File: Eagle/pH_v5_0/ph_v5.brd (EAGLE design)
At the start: 100 x 84.6 mm, 101 parts, among them CON1 JACK_DC_BARREL, IC1 MCP1703DB, J1 RJ12RIGHTANGLE-I2C, J2 RJ12RIGHTANGLE-I2C, Q1 BSP75, Q2 BSP75, Q3 BSP75, Q4 BSP75, U1 HX711, U100 RN2483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

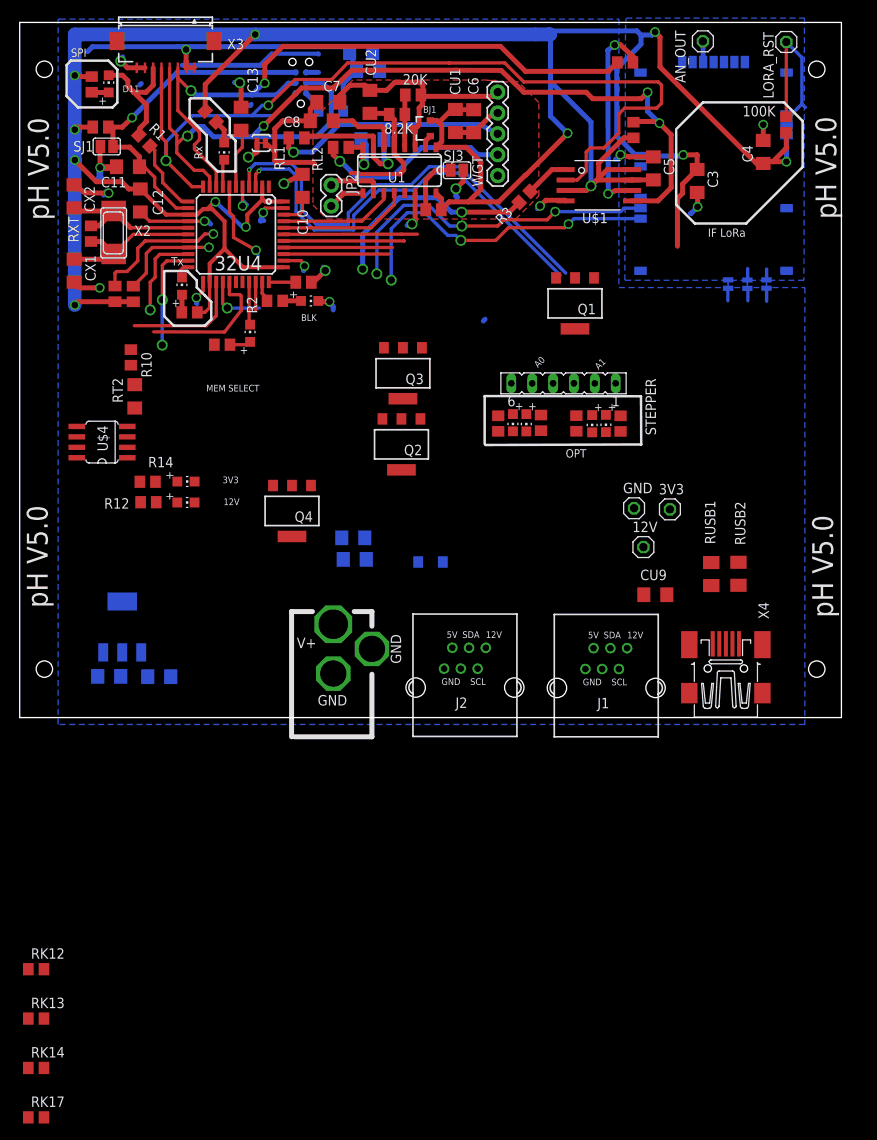
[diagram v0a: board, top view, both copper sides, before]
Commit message: started design of the phv5.0 board, conductommetry is still missing, stepper to be rerouted to use one single port would be better !
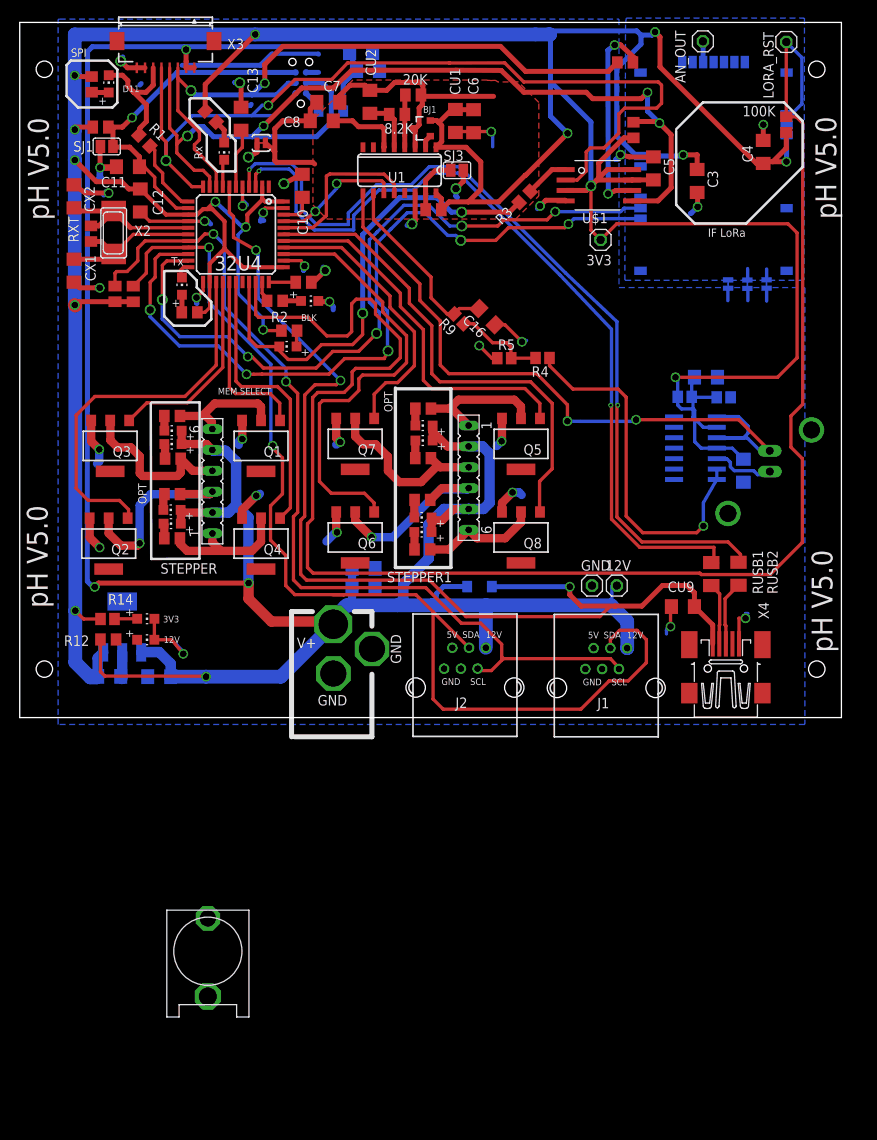
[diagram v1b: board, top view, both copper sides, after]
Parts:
- removed C9: 100nF, rcl:C1206
- removed JP2: (no value), SparkFun-Connectors:1X02
- removed R10: 1K, rcl:R0805
- removed RL1, RL2: 100, resistor:M0805
- removed RT2: 4.7k, resistor:R1206
- removed U$4: DS18B20, lpatiny:SO8
- removed WGT: (no value), SparkFun-Connectors:1X05
- added C14, C15: 100n, rcl:C1206
- added C16: 22uF, rcl:C1206
- added IC2: TL084D, linear:SO14
- added LDM5, LDM6, LDM7, LDM8: RED, adafruit:CHIP-LED0805
- added Q5, Q6, Q7, Q8: BSP75, infineon:PG-SOT-223
- added R4, R5, R9: 2.2k, resistor:R0805
- added R6, R8: 100k, resistor:R0805
- added STEPPER1: (no value), con-lsta:FE06
- added U$2: BNC-VERTICAL, phMeter:BNC-VERTICAL
- added U$3: VERTICAL-JACK, phMeter:VERTICAL-JACK
- moved RK14 83.6 mm to (44.0, 23.6), turned to 180 degrees
- moved RK17 83.6 mm to (44.0, 17.6), turned to 180 degrees
- moved RK12 82.9 mm to (44.1, 34.7), turned to 180 degrees
- moved RK13 82.9 mm to (44.1, 28.7), turned to 180 degrees
- moved RK8 56.3 mm to (13.5, 18.9), turned to 180 degrees
- moved LDM4 54.2 mm to (13.6, 20.7), turned to 90 degrees
- moved LDM3 52.2 mm to (13.5, 22.4), turned to 90 degrees
- moved RK9 49.9 mm to (13.6, 24.3), turned to 180 degrees
- moved RK10 45.0 mm to (13.6, 28.6), turned to 180 degrees
- moved STEPPER 44.4 mm to (18.4, 25.9), turned to 90 degrees
- moved LDM2 43.1 mm to (13.6, 30.4), turned to 90 degrees
- moved Q1 42.0 mm to (24.4, 30.2)
- moved LDM1 41.4 mm to (13.7, 32.0), turned to 90 degrees
- moved RK11 39.7 mm to (13.6, 33.8), turned to 180 degrees
- moved Q2 37.6 mm to (5.82, 18.3)
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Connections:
- removed net 5: J1.+5V, J2.+5V
- removed net N$20: C9.2, RL1.1, U1.7
- removed net N$43: C9.1, RL2.1, U1.8
- new net N$11: LDM6.C, RK13.2
- new net N$12: LDM7.C, RK14.2
- new net N$13: LDM8.C, RK17.2
- new net N$17: R4.2, R5.2, R9.1
- new net N$2: Q5.2, RK12.1, STEPPER1.1
- new net N$21: IC2.5, U$2.S
- new net N$27: C15.2, IC2.2, R6.1, R8.2
- new net N$28: IC2.6, IC2.7, R4.1
- new net N$4: Q7.2, RK13.1, STEPPER1.3
- new net N$6: Q6.2, RK14.1, STEPPER1.4
- new net N$8: Q8.2, RK17.1, STEPPER1.6
- net +12V: now also LDM5.A, LDM6.A, LDM7.A, LDM8.A, STEPPER1.2, STEPPER1.5
- net 3.3V: now also C14.1, IC2.4, R6.2; no longer RT2.1, U$4.3
- net A+: now also U1.8; no longer RL2.2, WGT.2
- net A-: now also U1.7; no longer RL1.2, WGT.3
- net A0: now also Q6.1; no longer Q2.1, RK13.2
- net A1: now also Q7.1; no longer Q4.1, RK17.2
- net A2: now also Q5.1; no longer Q3.1, RK14.2
- net A3: now also Q8.1; no longer Q1.1, RK12.2
- net A6: now also Q2.1
- net B+: now also C16.2, R9.2; no longer JP2.1
- net B-: now also IC2.1, IC2.3, U$2.G; no longer JP2.2
- net D12*: now also Q3.1
- net D6*: now also Q1.1; no longer R10.1
- net D8*: now also Q4.1
- net GND: now also C14.2, C15.1, C16.1, IC2.11, Q5.3, Q6.3, Q7.3, Q8.3, R5.1, R8.1; no longer RK12.1, RK13.1, RK14.1, RK17.1, U$4.5, WGT.1, WGT.4
- net N$5: no longer WGT.5
- net N$9: now also LDM5.C, RK12.2; no longer R10.2, RT2.2, U$4.4
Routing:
- net +12V: track 44.0 -> 323.9 mm, vias 1 -> 4
- net D5*: track 23.8 -> 202.5 mm
- net 3.3V: track 351.4 -> 491.0 mm, vias 12 -> 15
- net VUSB: track 10.2 -> 132.4 mm, vias 1 -> 3
- net SDA: track 12.6 -> 134.2 mm, vias 1 -> 2
- net SCL: track 16.6 -> 112.1 mm, vias 1 -> 2
- net B-: track 4.50 -> 86.8 mm, vias 0 -> 2
- net GND: track 105.7 -> 167.8 mm, vias 18 -> 32
- net USB_P: track 55.6 -> 106.2 mm, vias 1 -> 2
- net USB_N: track 53.6 -> 101.9 mm, vias 1 -> 2
- net N$28: track 0.00 -> 44.3 mm, vias 0 -> 1
- net RX: track 50.7 -> 94.6 mm, vias 4 -> 5
- net A3: track 16.3 -> 59.6 mm
- net A0: track 12.8 -> 54.9 mm
- net TX: track 53.5 -> 88.9 mm
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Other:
- board text removed: "A0"
- board text removed: "A1"

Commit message: ph board v5, need to be checked, to provide pin mapping and gerbers
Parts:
- removed RK15: 10k, rcl:R0805
- removed SJ5: (no value), SparkFun-Passives:PAD-JUMPER-2-NC_BY_TRACE_YES_SILK
- removed TXLD: RED, adafruit:CHIP-LED0805
- added B1: MB1S, rectifier:SOIC-4
- added C17, C18, C19, C20, C24, C9: 100nF, SparkysWidgets:1206
- added C21, C22, C23: 1uF, SparkysWidgets:1206
- added D3, D5: 4148, SparkysWidgets:SOD123
- added IC3: TL084D, linear:SO14
- added IC5: TPS60400DBV, SparkysWidgets:SOT23-DBV
- added R10: 22K, SparkysWidgets:0805
- added R11, R13, R15, R16, R17, R18, R20, R21, R22, R23, R24: 1K, SparkysWidgets:0805
- added R19: 1k, resistor:R0805
- added R7: 10K, SparkysWidgets:0805
- added TP5: OSCVout, SW_Passives:PAD.03X.03
- added U$5: BNC-VERTICAL, phMeter:BNC-VERTICAL
- moved U$3 85.4 mm to (87.3, 15.7)
- moved 3V3 26.2 mm to (57.9, 80.2)
- moved SJ6 18.0 mm to (68.3, 53.7), turned to 180 degrees
- moved SJ4 16.5 mm to (68.2, 56.0), turned to 180 degrees
- moved IC2 9.72 mm to (70.3, 23.1)
- moved C14 9.03 mm to (76.4, 21.1)
- moved C15 8.70 mm to (81.3, 30.3)
- moved R8 8.14 mm to (81.7, 28.0)
- moved R6 6.98 mm to (77.3, 29.3), turned to 90 degrees
- moved R4 5.04 mm to (53.6, 40.8)
- moved R5 4.71 mm to (49.3, 40.8)
- moved RUSB1 2.55 mm to (80.3, 12.3)
- moved RUSB2 2.55 mm to (83.6, 12.3)
- moved U$2 2.52 mm to (78.3, 32.5)
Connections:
- removed net A-: U1.7
- new net -3V3: C22.2, IC3.11, IC5.1
- new net N$20: C9.1, R13.1
- new net N$26: C19.1, IC3.1, R10.2, R13.2, R15.1
- new net N$29: IC3.5, R15.2, R16.1, TP5.P$1
- new net N$30: C17.2, C9.2, IC3.3, R11.2
- new net N$35: IC3.6, R18.1, U$5.S
- new net N$36: C24.1, IC3.7, R18.2
- new net N$40: C24.2, IC3.10, R20.2
- new net N$43: B1.~2, IC3.8
- new net N$44: C19.2, D3.C, D5.A
- new net N$45: C21.1, IC5.3
- new net N$46: C21.2, IC5.5
- new net N$47: B1.-, C18.1, R17.1, R23.1
- new net N$48: B1.~1, IC3.9, R21.1
- new net N$49: B1.+, C18.2, R17.2, R22.1
- new net N$50: IC3.12, R22.2
- new net N$51: IC3.13, R23.2, R24.2
- net 3.3V: now also C20.1, C23.1, IC3.4, IC5.2, U$3.P$1; no longer RK15.1
- net A+: now also IC3.14, R24.1
- net A4: now also R19.1, U$3.P$2; no longer U1.12
- net ANGND: no longer SJ5.2
- net D7*: now also U1.12
- net D8*: no longer Q4.1
- net GND: now also C17.1, C20.2, C22.1, C23.2, IC5.4, R11.1, R16.2, R19.2, R20.1, R21.2, R7.1, U$5.G; no longer SJ5.1
- net LGND: now also U1.7
- net N$18: now also D3.A, D5.C, IC3.2, R10.1, R7.2; no longer RK15.2, TXLD.A
- net TXLED: now also Q4.1; no longer TXLD.C
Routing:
- net A4: track 20.5 -> 115.0 mm, vias 0 -> 3
- net A+: track 0.00 -> 52.8 mm, vias 0 -> 3
- net GND: track 167.8 -> 206.8 mm, vias 32 -> 35
- net N$29: track 0.00 -> 38.4 mm
- net TXLED: track 2.01 -> 39.1 mm, vias 0 -> 2
- net 3.3V: track 491.0 -> 526.2 mm, vias 15 -> 17
- net D8*: track 34.6 -> 0.00 mm
- net N$48: track 0.00 -> 27.4 mm, vias 0 -> 1
- net N$43: track 0.00 -> 26.7 mm, vias 0 -> 1
- net N$35: track 0.00 -> 22.8 mm, vias 0 -> 1
- net ANGND: track 7.79 -> 28.4 mm
- net D7*: track 0.00 -> 19.9 mm
- net B-: track 86.8 -> 106.1 mm
- net N$51: track 0.00 -> 17.2 mm, vias 0 -> 1
- net N$18: track 2.17 -> 18.7 mm
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
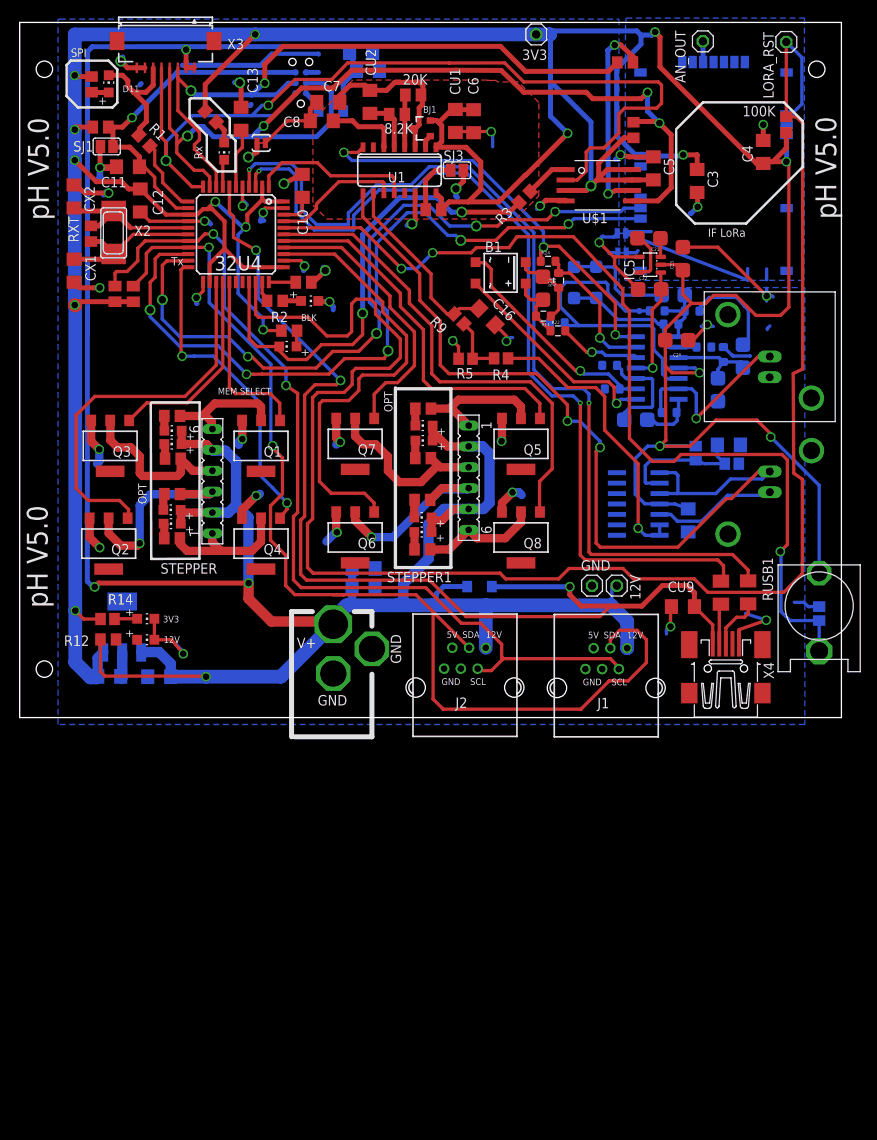
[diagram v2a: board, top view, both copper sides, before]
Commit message: finished phv5.0 board, need to dimension correctly the pH resistors and conductometry resistors and capa (not dimensionned yet !! careful not to solder anything)
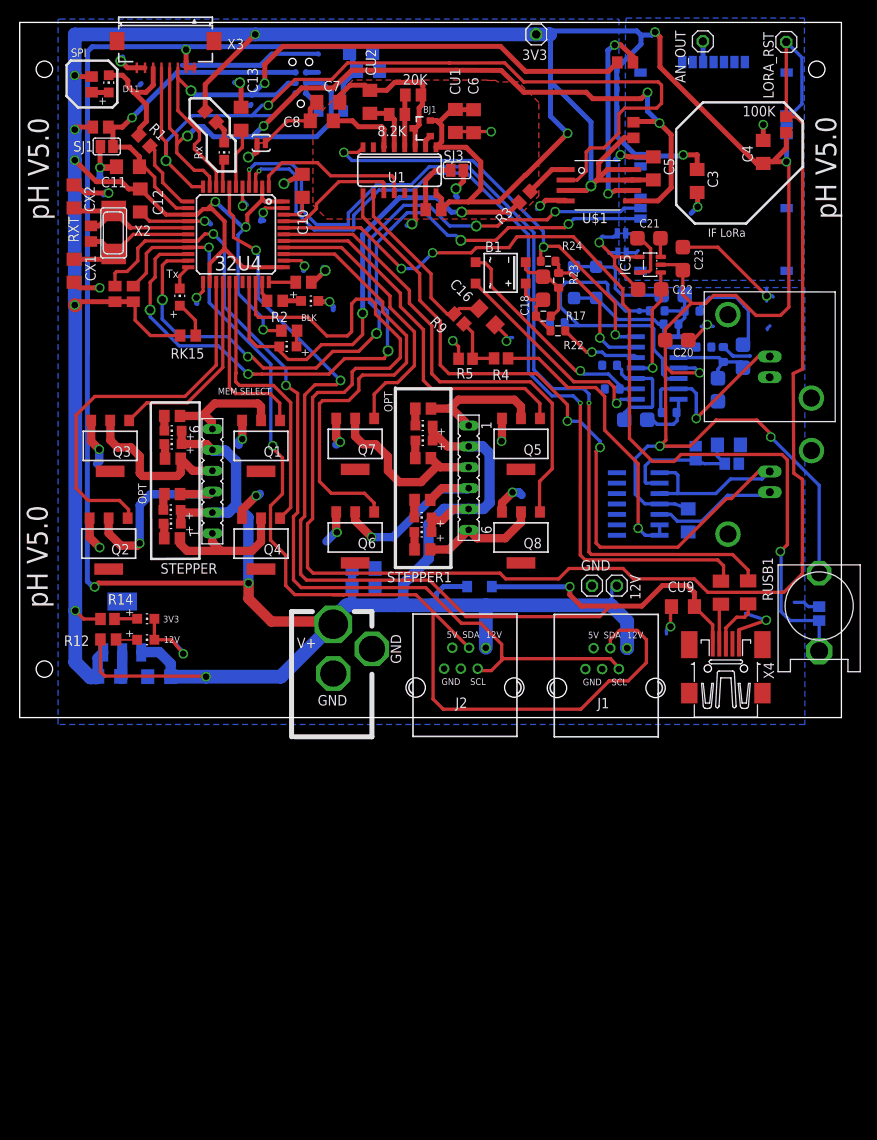
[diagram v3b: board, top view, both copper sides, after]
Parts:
- added RK15: 10k, rcl:R0805
- added RXLD1: RED, adafruit:CHIP-LED0805
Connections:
- new net N$52: RK15.2, RXLD1.A
- net 3.3V: now also RK15.1
- net D8*: now also Q4.1
- net TXLED: now also RXLD1.C; no longer Q4.1
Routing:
- net TXLED: track 39.1 -> 3.01 mm, vias 2 -> 0
- net D8*: track 0.00 -> 34.5 mm
- net ANGND: track 28.4 -> 7.38 mm
- net 3.3V: track 526.2 -> 535.0 mm
- net N$52: track 0.00 -> 4.51 mm
- net N$7: track 0.00 -> 2.57 mm
- net GND: track 206.8 -> 205.2 mm
